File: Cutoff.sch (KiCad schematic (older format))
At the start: 8 parts, among them Q1 Q_NMOS_DGS, Q2 Q_NMOS_DGS, U1 LTC4365DDB

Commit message: fixed pcb layout
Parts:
- R1, R2, R3, R4: footprint Resistor_SMD:R_0805_2012Metric_Pad1.20x1.40mm_HandSolder -> Resistor_SMD:R_0805_2012Metric_Pad1.15x1.40mm_HandSolder
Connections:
- net ov_sense: now reaches R2.2, R3.1, U1.2 (OV)
- net uv_sense: now reaches R1.2, R2.1, U1.3 (UV)
- net Vin renamed vin
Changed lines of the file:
@@
 Comment4 ""
 $EndDescr
-$Comp
-L Power_Management:LTC4365DDB U?
-U 1 1 602CD1DE
-P 5750 4100
-AR Path="/602CD1DE" Ref="U?"  Part="1"
-AR Path="/602C82B2/602CD1DE" Ref="U1"  Part="1"
-F 0 "U1" H 5750 4681 50  0000 C CNN
-F 1 "LTC4365DDB" H 5750 4590 50  0000 C CNN
-F 2 "Package_DFN_QFN:DFN-8-1EP_2x3mm_P0.5mm_EP0.61x2.2mm" H 5750 3600 50  0001 C CNN
-F 3 "https://www.analog.com/media/en/technical-documentation/data-sheets/4365fa.pdf" H 5750 4200 50  0001 C CNN
-	1    5750 4100
-	1    0    0    -1
-$EndComp
 Wire Wire Line
 	5350 3900 4900 3900
@@
 $Comp
 L power:GND #PWR?
-U 1 1 602CD201
-P 5800 4600
-AR Path="/602CD201" Ref="#PWR?"  Part="1"
-AR Path="/602C82B2/602CD201" Ref="#PWR0103"  Part="1"
-F 0 "#PWR0103" H 5800 4350 50  0001 C CNN
-F 1 "GND" H 5805 4427 50  0000 C CNN
-F 2 "" H 5800 4600 50  0001 C CNN
-F 3 "" H 5800 4600 50  0001 C CNN
-	1    5800 4600
-	1    0    0    -1
-$EndComp
-Wire Wire Line
-	5750 4500 5800 4500
-Wire Wire Line
-	5800 4500 5800 4600
-Connection ~ 5800 4500
-Wire Wire Line
-	5800 4500 5850 4500
-$Comp
-L power:GND #PWR?
 U 1 1 602CD20B
 P 4700 5050
@@
 F 0 "R3" H 4770 4946 50  0000 L CNN
 F 1 "100k" H 4770 4855 50  0000 L CNN
-F 2 "Resistor_SMD:R_0805_2012Metric_Pad1.20x1.40mm_HandSolder" V 4630 4900 50  0001 C CNN
+F 2 "Resistor_SMD:R_0805_2012Metric_Pad1.15x1.40mm_HandSolder" V 4630 4900 50  0001 C CNN
 F 3 "~" H 4700 4900 50  0001 C CNN
 	1    4700 4900
@@
 F 0 "R4" H 5220 4046 50  0000 L CNN
 F 1 "100k" H 5220 3955 50  0000 L CNN
-F 2 "Resistor_SMD:R_0805_2012Metric_Pad1.20x1.40mm_HandSolder" V 5080 4000 50  0001 C CNN
+F 2 "Resistor_SMD:R_0805_2012Metric_Pad1.15x1.40mm_HandSolder" V 5080 4000 50  0001 C CNN
 F 3 "~" H 5150 4000 50  0001 C CNN
 	1    5150 4000
@@
 F 0 "R2" H 4770 4546 50  0000 L CNN
 F 1 "200k" H 4770 4455 50  0000 L CNN
-F 2 "Resistor_SMD:R_0805_2012Metric_Pad1.20x1.40mm_HandSolder" V 4630 4500 50  0001 C CNN
+F 2 "Resistor_SMD:R_0805_2012Metric_Pad1.15x1.40mm_HandSolder" V 4630 4500 50  0001 C CNN
 F 3 "~" H 4700 4500 50  0001 C CNN
 	1    4700 4500
@@
 F 0 "R1" H 4770 4146 50  0000 L CNN
 F 1 "2.7M" H 4770 4055 50  0000 L CNN
-F 2 "Resistor_SMD:R_0805_2012Metric_Pad1.20x1.40mm_HandSolder" V 4630 4100 50  0001 C CNN
+F 2 "Resistor_SMD:R_0805_2012Metric_Pad1.15x1.40mm_HandSolder" V 4630 4100 50  0001 C CNN
 F 3 "~" H 4700 4100 50  0001 C CNN
 	1    4700 4100
@@
 $EndComp
 Text HLabel 4700 3300 0    50   Input ~ 0
-Vin
+vin
 Text HLabel 7350 3300 2    50   Output ~ 0
 Vout
@@
 Wire Wire Line
 	6350 3300 6650 3300
+Wire Wire Line
+	5800 4500 5850 4500
+Wire Wire Line
+	5750 4500 5800 4500
+Connection ~ 5800 4500
+Wire Wire Line
+	5800 4500 5800 4600
+$Comp
+L power:GND #PWR?
+U 1 1 602CD201
+P 5800 4600
+AR Path="/602CD201" Ref="#PWR?"  Part="1"
+AR Path="/602C82B2/602CD201" Ref="#PWR0103"  Part="1"
+F 0 "#PWR0103" H 5800 4350 50  0001 C CNN
+F 1 "GND" H 5805 4427 50  0000 C CNN
+F 2 "" H 5800 4600 50  0001 C CNN
+F 3 "" H 5800 4600 50  0001 C CNN
+	1    5800 4600
+	1    0    0    -1
+$EndComp
+$Comp
+L Power_Management:LTC4365DDB U?
+U 1 1 602CD1DE
+P 5750 4100
+AR Path="/602CD1DE" Ref="U?"  Part="1"
+AR Path="/602C82B2/602CD1DE" Ref="U1"  Part="1"
+F 0 "U1" H 5750 4681 50  0000 C CNN
+F 1 "LTC4365DDB" H 5750 4590 50  0000 C CNN
+F 2 "Package_DFN_QFN:DFN-8-1EP_2x3mm_P0.5mm_EP0.61x2.2mm" H 5750 3600 50  0001 C CNN
+F 3 "https://www.analog.com/media/en/technical-documentation/data-sheets/4365fa.pdf" H 5750 4200 50  0001 C CNN
+	1    5750 4100
+	1    0    0    -1
+$EndComp
+Text Label 4900 4300 0    50   ~ 0
+uv_sense
+Text Label 4900 4700 0    50   ~ 0
+ov_sense
+Text Label 5000 3900 0    50   ~ 0
+vin
 $EndSCHEMATC

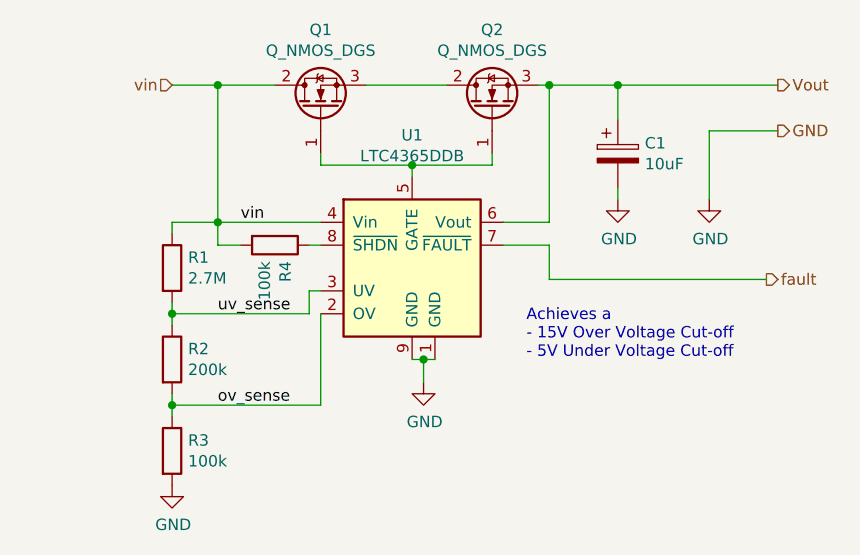
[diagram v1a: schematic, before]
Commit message: added new heatsink alterantive
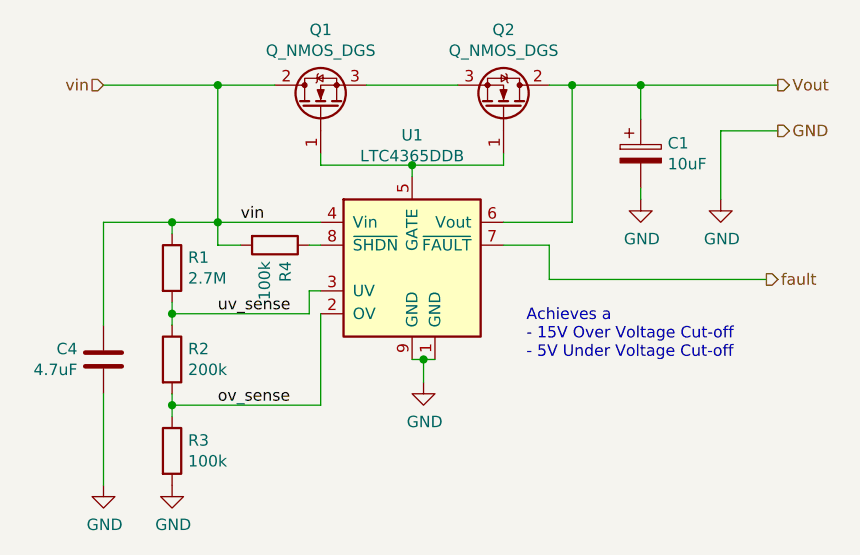
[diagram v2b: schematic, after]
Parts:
- added C4: 4.7uF, Capacitor_SMD:C_0805_2012Metric_Pad1.18x1.45mm_HandSolder, symbol Device:C
- C1: footprint Capacitor_Tantalum_SMD:CP_EIA-3216-12_Kemet-S_Pad1.58x1.35mm_HandSolder -> Capacitor_SMD:C_0805_2012Metric_Pad1.18x1.45mm_HandSolder; dk_pn (none) -> 1276-2891-1-ND
- Q1, Q2: dk_pn (none) -> 742-SUD19N20-90-BE3CT-ND; ms_pn (none) -> 78-SUD19N20-90-BE3
- R1: dk_pn (none) -> 408-2157-1-ND; ms_pn (none) -> 754-RGT2012P-275BT5
- R2: dk_pn (none) -> P200KDACT-ND; ms_pn (none) -> 71-RCC0805200KFKEA
- R3, R4: dk_pn (none) -> P100KDACT-ND; ms_pn (none) -> 603-AT0805FRE07100KL
- U1: dk_pn (none) -> LTC4365HDDB-1#TRMPBFCT-ND; ms_pn (none) -> 584-C4365HDDB-1TMPF
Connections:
- net GND: now also C4.1
- net Vout: now also Q2.2 (D); no longer Q2.3 (S)
- net vin: now also C4.2
- net at Q1.3 (S): now also Q2.3 (S); no longer Q2.2 (D)
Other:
- moved on the sheet: C1, Q2
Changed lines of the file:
@@
 Connection ~ 5750 3650
 Wire Wire Line
-	5750 3650 6100 3650
+	5750 3650 6150 3650
 Wire Wire Line
 	5150 3300 4900 3300
@@
 Connection ~ 4900 3900
 Wire Wire Line
-	6100 3650 6100 3600
-Wire Wire Line
-	5550 3300 5900 3300
+	6150 3650 6150 3600
+Wire Wire Line
+	5550 3300 5950 3300
 $Comp
 L Device:CP C?
 U 1 1 602CD1EF
-P 6650 3600
+P 6750 3600
 AR Path="/602CD1EF" Ref="C?"  Part="1"
 AR Path="/602C82B2/602CD1EF" Ref="C1"  Part="1"
-F 0 "C1" H 6768 3646 50  0000 L CNN
-F 1 "10uF" H 6768 3555 50  0000 L CNN
-F 2 "Capacitor_Tantalum_SMD:CP_EIA-3216-12_Kemet-S_Pad1.58x1.35mm_HandSolder" H 6688 3450 50  0001 C CNN
-F 3 "~" H 6650 3600 50  0001 C CNN
-	1    6650 3600
-	1    0    0    -1
-$EndComp
-Wire Wire Line
-	6300 3300 6350 3300
-Wire Wire Line
-	6650 3450 6650 3300
+F 0 "C1" H 6868 3646 50  0000 L CNN
+F 1 "10uF" H 6868 3555 50  0000 L CNN
+F 2 "Capacitor_SMD:C_0805_2012Metric_Pad1.18x1.45mm_HandSolder" H 6788 3450 50  0001 C CNN
+F 3 "~" H 6750 3600 50  0001 C CNN
+F 4 "" H 6750 3600 50  0001 C CNN "ms_pn"
+F 5 "1276-2891-1-ND" H 6750 3600 50  0001 C CNN "dk_pn"
+	1    6750 3600
+	1    0    0    -1
+$EndComp
+Wire Wire Line
+	6350 3300 6450 3300
+Wire Wire Line
+	6750 3450 6750 3300
 $Comp
 L power:GND #PWR?
 U 1 1 602CD1F7
-P 6650 3800
+P 6750 3800
 AR Path="/602CD1F7" Ref="#PWR?"  Part="1"
 AR Path="/602C82B2/602CD1F7" Ref="#PWR0102"  Part="1"
-F 0 "#PWR0102" H 6650 3550 50  0001 C CNN
-F 1 "GND" H 6655 3627 50  0000 C CNN
-F 2 "" H 6650 3800 50  0001 C CNN
-F 3 "" H 6650 3800 50  0001 C CNN
-	1    6650 3800
-	1    0    0    -1
-$EndComp
-Wire Wire Line
-	6650 3800 6650 3750
-Wire Wire Line
-	6150 3900 6350 3900
-Wire Wire Line
-	6350 3900 6350 3300
-Connection ~ 6350 3300
+F 0 "#PWR0102" H 6750 3550 50  0001 C CNN
+F 1 "GND" H 6755 3627 50  0000 C CNN
+F 2 "" H 6750 3800 50  0001 C CNN
+F 3 "" H 6750 3800 50  0001 C CNN
+	1    6750 3800
+	1    0    0    -1
+$EndComp
+Wire Wire Line
+	6750 3800 6750 3750
+Wire Wire Line
+	6150 3900 6450 3900
+Wire Wire Line
+	6450 3900 6450 3300
+Connection ~ 6450 3300
 $Comp
 L power:GND #PWR?
@@
 F 2 "Resistor_SMD:R_0805_2012Metric_Pad1.15x1.40mm_HandSolder" V 4630 4900 50  0001 C CNN
 F 3 "~" H 4700 4900 50  0001 C CNN
+F 4 "603-AT0805FRE07100KL" H 4700 4900 50  0001 C CNN "ms_pn"
+F 5 "P100KDACT-ND" H 4700 4900 50  0001 C CNN "dk_pn"
 	1    4700 4900
 	1    0    0    -1
@@
 F 2 "Resistor_SMD:R_0805_2012Metric_Pad1.15x1.40mm_HandSolder" V 5080 4000 50  0001 C CNN
 F 3 "~" H 5150 4000 50  0001 C CNN
+F 4 "603-AT0805FRE07100KL" H 5150 4000 50  0001 C CNN "ms_pn"
+F 5 "P100KDACT-ND" H 5150 4000 50  0001 C CNN "dk_pn"
 	1    5150 4000
 	0    1    1    0
@@
 Achieves a \n- 15V Over Voltage Cut-off\n- 5V Under Voltage Cut-off
 Wire Wire Line
-	7350 3500 7050 3500
-Wire Wire Line
-	7050 3500 7050 3800
+	7350 3500 7100 3500
+Wire Wire Line
+	7100 3500 7100 3800
 $Comp
 L power:GND #PWR?
 U 1 1 602CD227
-P 7050 3800
+P 7100 3800
 AR Path="/602CD227" Ref="#PWR?"  Part="1"
 AR Path="/602C82B2/602CD227" Ref="#PWR0105"  Part="1"
-F 0 "#PWR0105" H 7050 3550 50  0001 C CNN
-F 1 "GND" H 7055 3627 50  0000 C CNN
-F 2 "" H 7050 3800 50  0001 C CNN
-F 3 "" H 7050 3800 50  0001 C CNN
-	1    7050 3800
-	1    0    0    -1
-$EndComp
-Wire Wire Line
-	7350 3300 6650 3300
-Connection ~ 6650 3300
+F 0 "#PWR0105" H 7100 3550 50  0001 C CNN
+F 1 "GND" H 7105 3627 50  0000 C CNN
+F 2 "" H 7100 3800 50  0001 C CNN
+F 3 "" H 7100 3800 50  0001 C CNN
+	1    7100 3800
+	1    0    0    -1
+$EndComp
+Wire Wire Line
+	7350 3300 6750 3300
+Connection ~ 6750 3300
 Wire Wire Line
 	4700 3900 4900 3900
@@
 F 2 "Resistor_SMD:R_0805_2012Metric_Pad1.15x1.40mm_HandSolder" V 4630 4500 50  0001 C CNN
 F 3 "~" H 4700 4500 50  0001 C CNN
+F 4 "71-RCC0805200KFKEA" H 4700 4500 50  0001 C CNN "ms_pn"
+F 5 "P200KDACT-ND" H 4700 4500 50  0001 C CNN "dk_pn"
 	1    4700 4500
 	1    0    0    -1
@@
 F 2 "Resistor_SMD:R_0805_2012Metric_Pad1.15x1.40mm_HandSolder" V 4630 4100 50  0001 C CNN
 F 3 "~" H 4700 4100 50  0001 C CNN
+F 4 "754-RGT2012P-275BT5" H 4700 4100 50  0001 C CNN "ms_pn"
+F 5 "408-2157-1-ND" H 4700 4100 50  0001 C CNN "dk_pn"
 	1    4700 4100
 	1    0    0    -1
@@
 Connection ~ 4900 3300
 Wire Wire Line
-	4700 3300 4900 3300
+	4400 3300 4900 3300
 $Comp
 L Device:Q_NMOS_GDS Q?
@@
 F 2 "Package_TO_SOT_SMD:TO-252-2" H 5550 3500 50  0001 C CNN
 F 3 "~" H 5350 3400 50  0001 C CNN
+F 4 "78-SUD19N20-90-BE3" H 5350 3400 50  0001 C CNN "ms_pn"
+F 5 "742-SUD19N20-90-BE3CT-ND" H 5350 3400 50  0001 C CNN "dk_pn"
 	1    5350 3400
 	0    -1   -1   0
 $EndComp
-$Comp
-L Device:Q_NMOS_GDS Q?
-U 1 1 602CD259
-P 6100 3400
-AR Path="/602CD259" Ref="Q?"  Part="1"
-AR Path="/602C82B2/602CD259" Ref="Q2"  Part="1"
-F 0 "Q2" V 6442 3400 50  0000 C CNN
-F 1 "Q_NMOS_DGS" V 6351 3400 50  0000 C CNN
-F 2 "Package_TO_SOT_SMD:TO-252-2" H 6300 3500 50  0001 C CNN
-F 3 "~" H 6100 3400 50  0001 C CNN
-	1    6100 3400
-	0    -1   -1   0
-$EndComp
-Text HLabel 4700 3300 0    50   Input ~ 0
+Text HLabel 4400 3300 0    50   Input ~ 0
 vin
 Text HLabel 7350 3300 2    50   Output ~ 0
@@
 	6350 4000 6150 4000
 Wire Wire Line
-	6350 3300 6650 3300
+	6450 3300 6750 3300
 Wire Wire Line
 	5800 4500 5850 4500
@@
 F 2 "Package_DFN_QFN:DFN-8-1EP_2x3mm_P0.5mm_EP0.61x2.2mm" H 5750 3600 50  0001 C CNN
 F 3 "https://www.analog.com/media/en/technical-documentation/data-sheets/4365fa.pdf" H 5750 4200 50  0001 C CNN
+F 4 "584-C4365HDDB-1TMPF" H 5750 4100 50  0001 C CNN "ms_pn"
+F 5 "LTC4365HDDB-1#TRMPBFCT-ND" H 5750 4100 50  0001 C CNN "dk_pn"
 	1    5750 4100
 	1    0    0    -1
@@
 Text Label 5000 3900 0    50   ~ 0
 vin
+$Comp
+L Device:Q_NMOS_GDS Q?
+U 1 1 602CD259
+P 6150 3400
+AR Path="/602CD259" Ref="Q?"  Part="1"
+AR Path="/602C82B2/602CD259" Ref="Q2"  Part="1"
+F 0 "Q2" V 6492 3400 50  0000 C CNN
+F 1 "Q_NMOS_DGS" V 6401 3400 50  0000 C CNN
+F 2 "Package_TO_SOT_SMD:TO-252-2" H 6350 3500 50  0001 C CNN
+F 3 "~" H 6150 3400 50  0001 C CNN
+F 4 "78-SUD19N20-90-BE3" H 6150 3400 50  0001 C CNN "ms_pn"
+F 5 "742-SUD19N20-90-BE3CT-ND" H 6150 3400 50  0001 C CNN "dk_pn"
+	1    6150 3400
+	0    1    -1   0
+$EndComp
+$Comp
+L Device:C C4
+U 1 1 6034F4F1
+P 4400 4500
+F 0 "C4" H 4286 4454 50  0000 R CNN
+F 1 "4.7uF" H 4286 4545 50  0000 R CNN
+F 2 "Capacitor_SMD:C_0805_2012Metric_Pad1.18x1.45mm_HandSolder" H 4438 4350 50  0001 C CNN
+F 3 "~" H 4400 4500 50  0001 C CNN
+	1    4400 4500
+	1    0    0    1
+$EndComp
+Wire Wire Line
+	4400 4350 4400 3900
+Wire Wire Line
+	4400 3900 4700 3900
+Connection ~ 4700 3900
+$Comp
+L power:GND #PWR?
+U 1 1 60350A78
+P 4400 5050
+AR Path="/60350A78" Ref="#PWR?"  Part="1"
+AR Path="/602C82B2/60350A78" Ref="#PWR01"  Part="1"
+F 0 "#PWR01" H 4400 4800 50  0001 C CNN
+F 1 "GND" H 4405 4877 50  0000 C CNN
+F 2 "" H 4400 5050 50  0001 C CNN
+F 3 "" H 4400 5050 50  0001 C CNN
+	1    4400 5050
+	1    0    0    -1
+$EndComp
+Wire Wire Line
+	4400 4650 4400 5050
 $EndSCHEMATC

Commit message: changed layout for heat sink w/ issue #1
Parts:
- C1: ms_pn (none) -> 187-CL21A106KAYNNNE
- C4: dk_pn (none) -> 732-7628-1-ND; ms_pn (none) -> 710-885012107018
- R1: ms_pn 754-RGT2012P-275BT5 -> 603-RC0805FR-072M7L
- R3, R4: dk_pn P100KDACT-ND -> RMCF0805FT100KCT-ND; ms_pn 603-AT0805FRE07100KL -> 71-CRCW0805100KFKEBC
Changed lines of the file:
@@
 F 2 "Capacitor_SMD:C_0805_2012Metric_Pad1.18x1.45mm_HandSolder" H 6788 3450 50  0001 C CNN
 F 3 "~" H 6750 3600 50  0001 C CNN
-F 4 "" H 6750 3600 50  0001 C CNN "ms_pn"
+F 4 "187-CL21A106KAYNNNE" H 6750 3600 50  0001 C CNN "ms_pn"
 F 5 "1276-2891-1-ND" H 6750 3600 50  0001 C CNN "dk_pn"
 	1    6750 3600
@@
 F 2 "Resistor_SMD:R_0805_2012Metric_Pad1.15x1.40mm_HandSolder" V 4630 4900 50  0001 C CNN
 F 3 "~" H 4700 4900 50  0001 C CNN
-F 4 "603-AT0805FRE07100KL" H 4700 4900 50  0001 C CNN "ms_pn"
-F 5 "P100KDACT-ND" H 4700 4900 50  0001 C CNN "dk_pn"
+F 4 "71-CRCW0805100KFKEBC" H 4700 4900 50  0001 C CNN "ms_pn"
+F 5 "RMCF0805FT100KCT-ND" H 4700 4900 50  0001 C CNN "dk_pn"
 	1    4700 4900
 	1    0    0    -1
@@
 F 2 "Resistor_SMD:R_0805_2012Metric_Pad1.15x1.40mm_HandSolder" V 5080 4000 50  0001 C CNN
 F 3 "~" H 5150 4000 50  0001 C CNN
-F 4 "603-AT0805FRE07100KL" H 5150 4000 50  0001 C CNN "ms_pn"
-F 5 "P100KDACT-ND" H 5150 4000 50  0001 C CNN "dk_pn"
+F 4 "71-CRCW0805100KFKEBC" H 5150 4000 50  0001 C CNN "ms_pn"
+F 5 "RMCF0805FT100KCT-ND" H 5150 4000 50  0001 C CNN "dk_pn"
 	1    5150 4000
 	0    1    1    0
@@
 F 2 "Resistor_SMD:R_0805_2012Metric_Pad1.15x1.40mm_HandSolder" V 4630 4100 50  0001 C CNN
 F 3 "~" H 4700 4100 50  0001 C CNN
-F 4 "754-RGT2012P-275BT5" H 4700 4100 50  0001 C CNN "ms_pn"
+F 4 "603-RC0805FR-072M7L" H 4700 4100 50  0001 C CNN "ms_pn"
 F 5 "408-2157-1-ND" H 4700 4100 50  0001 C CNN "dk_pn"
 	1    4700 4100
@@
 F 2 "Capacitor_SMD:C_0805_2012Metric_Pad1.18x1.45mm_HandSolder" H 4438 4350 50  0001 C CNN
 F 3 "~" H 4400 4500 50  0001 C CNN
+F 4 "732-7628-1-ND" H 4400 4500 50  0001 C CNN "dk_pn"
+F 5 "710-885012107018" H 4400 4500 50  0001 C CNN "ms_pn"
 	1    4400 4500
 	1    0    0    1
